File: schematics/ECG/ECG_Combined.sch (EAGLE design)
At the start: 76 parts, among them IC1 ADS1293, IC2 LIS3DH, IC3 MCP1703, IC4 CC2541, IC5 FSA4157, IC6 FSA4157, IC7 FSA4157, X1 XTAL-2SMD, X2 XTAL_403, X3 XTAL-CSM7

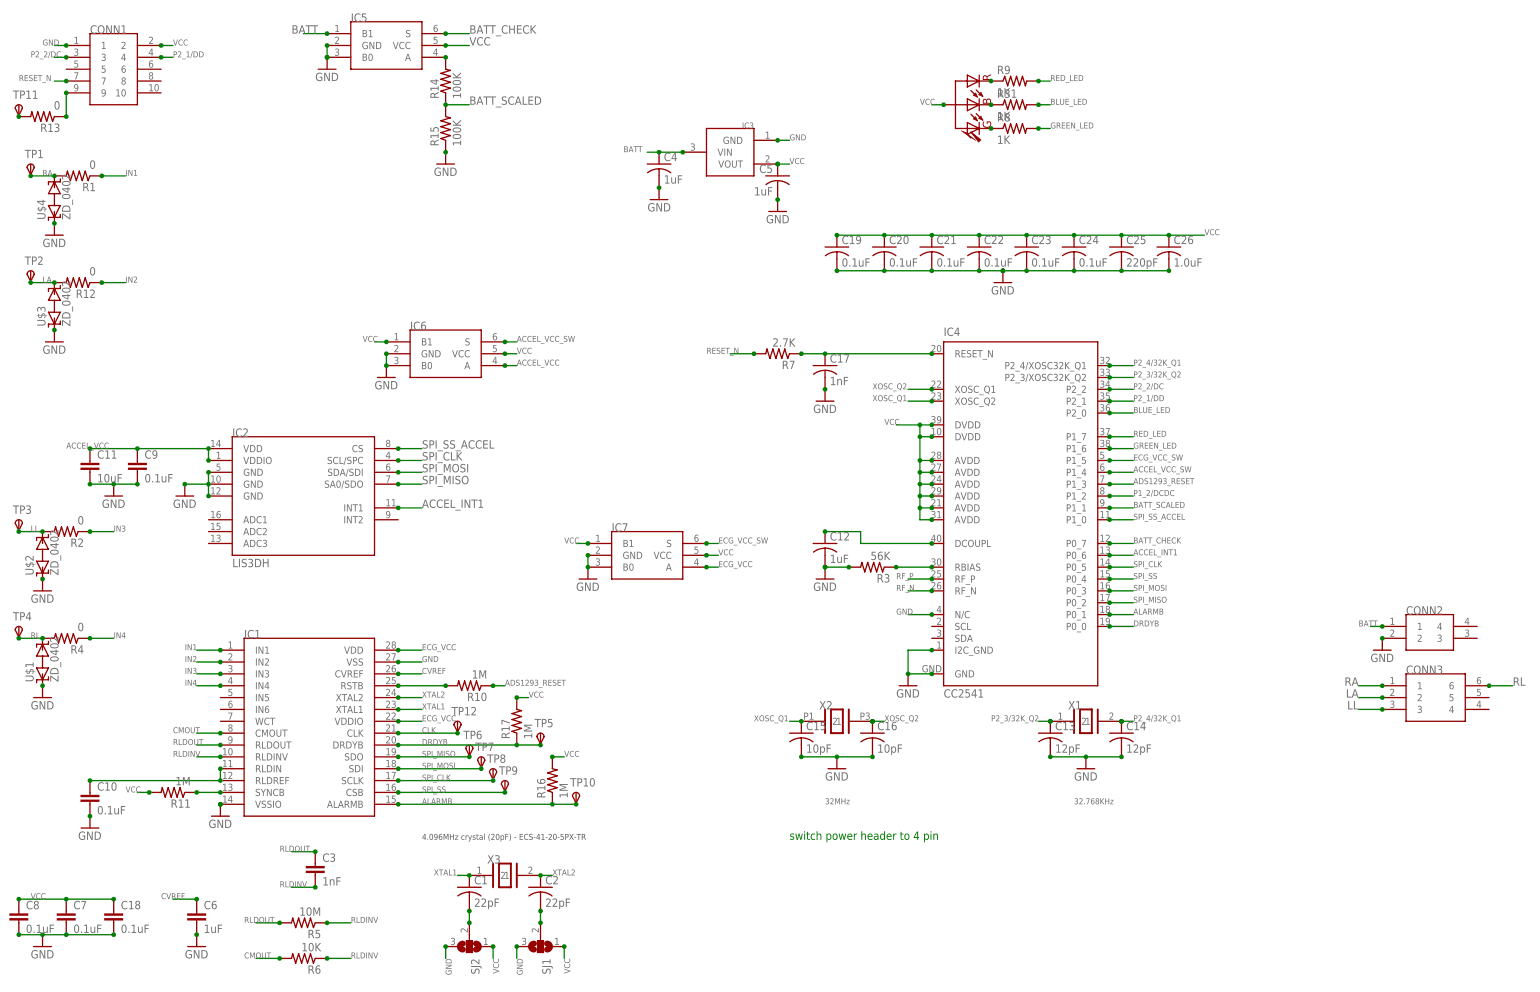
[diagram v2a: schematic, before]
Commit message: removed cc2541 ground on pin 4. added balun and antenna
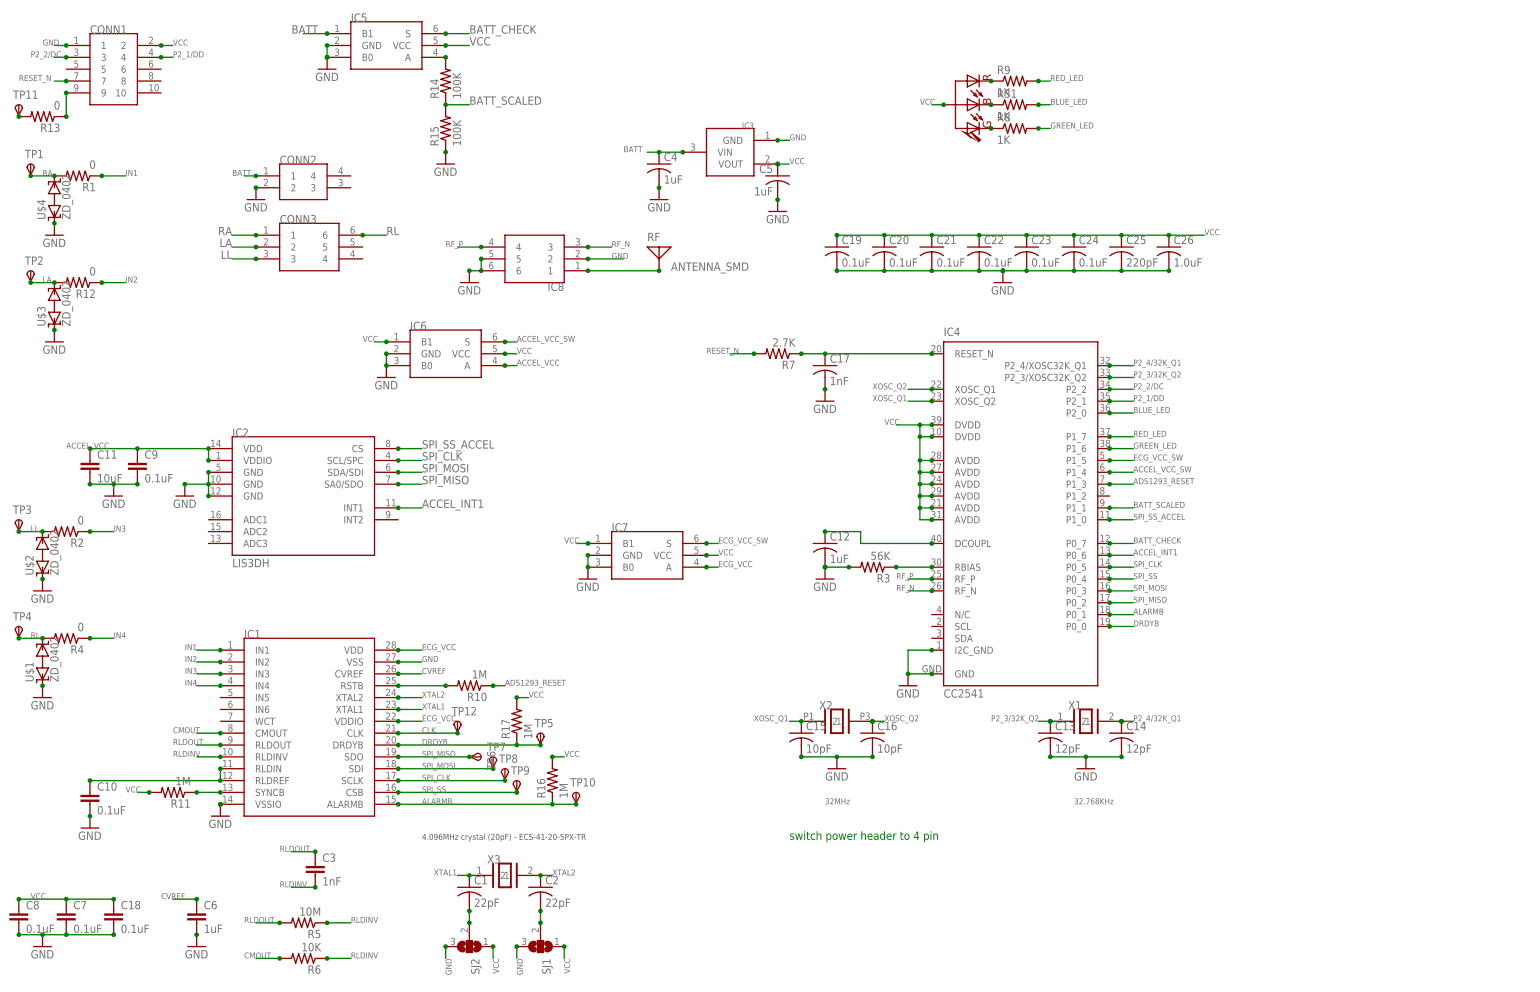
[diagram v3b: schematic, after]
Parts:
- added IC8: BALUN_2450BM_SERIES_SMD, johanson:BALUN_2450BM_SERIES_SMD
- added RF: ANTENNA_SMD, johanson:ANTENNA_SMD
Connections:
- net DCOUPL1 renamed DCOUPL
- removed net P1_2/DCDC: IC4.P1_2
- new net N$6: IC8.1, RF.1
- net GND: now also IC8.2, IC8.5, IC8.6; no longer IC4.N/C
- net RF_N: now also IC8.3
- net RF_P: now also IC8.4
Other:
- moved on the sheet: CONN2, CONN3, TP6, TP7, TP8, TP9
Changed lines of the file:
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@@
 <part name="GND20" library="supply1" deviceset="GND" device=""/>
 <part name="GND23" library="supply1" deviceset="GND" device=""/>
+<part name="RF" library="johanson" deviceset="ANTENNA_SMD" device=""/>
+<part name="IC8" library="johanson" deviceset="BALUN_2450BM_SERIES_SMD" device="" value=""/>
+<part name="GND24" library="supply1" deviceset="GND" device=""/>
 </parts>
 <sheets>
@@
 <instance part="TP4" gate="G$1" x="10.16" y="78.74"/>
 <instance part="TP5" gate="G$1" x="121.92" y="55.88"/>
-<instance part="TP6" gate="G$1" x="106.68" y="53.34"/>
-<instance part="TP7" gate="G$1" x="109.22" y="50.8"/>
-<instance part="TP8" gate="G$1" x="111.76" y="48.26"/>
-<instance part="TP9" gate="G$1" x="114.3" y="45.72"/>
+<instance part="TP6" gate="G$1" x="109.22" y="50.8" rot="R270"/>
+<instance part="TP7" gate="G$1" x="111.76" y="50.8"/>
+<instance part="TP8" gate="G$1" x="114.3" y="48.26"/>
+<instance part="TP9" gate="G$1" x="116.84" y="45.72"/>
 <instance part="TP10" gate="G$1" x="129.54" y="43.18"/>
 <instance part="R13" gate="G$1" x="15.24" y="187.96" rot="R180"/>
@@
 <instance part="R15" gate="G$1" x="101.6" y="185.42" rot="R90"/>
 <instance part="GND22" gate="1" x="101.6" y="177.8"/>
-<instance part="CONN3" gate="CONN" x="312.42" y="63.5"/>
+<instance part="CONN3" gate="CONN" x="71.12" y="160.02"/>
 <instance part="R1" gate="G$1" x="22.86" y="175.26" rot="R180"/>
 <instance part="R12" gate="G$1" x="22.86" y="152.4" rot="R180"/>
@@
 <instance part="TRI_LED" gate="LED" x="213.36" y="190.5" rot="R90"/>
 <instance part="R9" gate="G$1" x="223.52" y="195.58"/>
-<instance part="CONN2" gate="CONN" x="312.42" y="76.2"/>
-<instance part="GND17" gate="1" x="302.26" y="73.66"/>
+<instance part="CONN2" gate="CONN" x="71.12" y="172.72"/>
+<instance part="GND17" gate="1" x="60.96" y="170.18"/>
 <instance part="U$1" gate="Z" x="15.24" y="71.12" rot="R90"/>
 <instance part="U$2" gate="Z" x="15.24" y="93.98" rot="R90"/>
@@
 <instance part="GND20" gate="1" x="15.24" y="86.36"/>
 <instance part="GND23" gate="1" x="15.24" y="63.5"/>
+<instance part="RF" gate="RF" x="147.32" y="154.94"/>
+<instance part="IC8" gate="IC" x="121.92" y="157.48" rot="R180"/>
+<instance part="GND24" gate="1" x="106.68" y="152.4"/>
 </instances>
 <busses>
@@
 <junction x="205.74" y="73.66"/>
 <junction x="205.74" y="68.58"/>
-</segment>
-<segment>
-<pinref part="IC4" gate="G$1" pin="N/C"/>
-<junction x="205.74" y="81.28"/>
-<wire x1="205.74" y1="81.28" x2="200.66" y2="81.28" width="0.1524" layer="91"/>
-<label x="198.12" y="81.28" size="1.27" layer="95"/>
 </segment>
 <segment>
@@
 <pinref part="CONN2" gate="CONN" pin="2"/>
 <pinref part="GND17" gate="1" pin="GND"/>
-<junction x="302.26" y="76.2"/>
+<junction x="60.96" y="172.72"/>
 </segment>
 <segment>
@@
 <pinref part="GND23" gate="1" pin="GND"/>
 <junction x="15.24" y="66.04"/>
+</segment>
+<segment>
+<wire x1="109.22" y1="157.48" x2="109.22" y2="154.94" width="0.1524" layer="91"/>
+<wire x1="109.22" y1="154.94" x2="106.68" y2="154.94" width="0.1524" layer="91"/>
+<junction x="109.22" y="154.94"/>
+<junction x="109.22" y="157.48"/>
+<junction x="106.68" y="154.94"/>
+<pinref part="IC8" gate="IC" pin="5"/>
+<pinref part="IC8" gate="IC" pin="6"/>
+<pinref part="GND24" gate="1" pin="GND"/>
+</segment>
+<segment>
+<wire x1="132.08" y1="157.48" x2="139.7" y2="157.48" width="0.1524" layer="91"/>
+<junction x="132.08" y="157.48"/>
+<label x="137.16" y="157.48" size="1.27" layer="95"/>
+<pinref part="IC8" gate="IC" pin="2"/>
 </segment>
 </net>
@@
 <segment>
 <pinref part="CONN3" gate="CONN" pin="1"/>
-<junction x="302.26" y="66.04"/>
-<wire x1="302.26" y1="66.04" x2="297.18" y2="66.04" width="0.1524" layer="91"/>
-<label x="297.18" y="66.04" size="1.778" layer="95" rot="MR0"/>
+<junction x="60.96" y="162.56"/>
+<wire x1="60.96" y1="162.56" x2="55.88" y2="162.56" width="0.1524" layer="91"/>
+<label x="55.88" y="162.56" size="1.778" layer="95" rot="MR0"/>
 </segment>
 </net>
@@
 <segment>
 <pinref part="CONN3" gate="CONN" pin="3"/>
-<junction x="302.26" y="60.96"/>
-<wire x1="302.26" y1="60.96" x2="297.18" y2="60.96" width="0.1524" layer="91"/>
-<label x="297.18" y="60.96" size="1.778" layer="95" rot="MR0"/>
+<junction x="60.96" y="157.48"/>
+<wire x1="60.96" y1="157.48" x2="55.88" y2="157.48" width="0.1524" layer="91"/>
+<label x="55.88" y="157.48" size="1.778" layer="95" rot="MR0"/>
 </segment>
 </net>
@@
 <segment>
 <pinref part="CONN3" gate="CONN" pin="6"/>
-<junction x="325.12" y="66.04"/>
-<wire x1="325.12" y1="66.04" x2="330.2" y2="66.04" width="0.1524" layer="91"/>
-<label x="330.2" y="66.04" size="1.778" layer="95"/>
+<junction x="83.82" y="162.56"/>
+<wire x1="83.82" y1="162.56" x2="88.9" y2="162.56" width="0.1524" layer="91"/>
+<label x="88.9" y="162.56" size="1.778" layer="95"/>
 </segment>
 </net>
@@
 </segment>
 </net>
-<net name="DCOUPL1" class="0">
+<net name="DCOUPL" class="0">
 <segment>
 <pinref part="IC4" gate="G$1" pin="DCOUPL"/>
@@
 <label x="198.12" y="86.36" size="1.27" layer="95"/>
 </segment>
+<segment>
+<wire x1="137.16" y1="160.02" x2="132.08" y2="160.02" width="0.1524" layer="91"/>
+<junction x="132.08" y="160.02"/>
+<pinref part="IC8" gate="IC" pin="3"/>
+<label x="137.16" y="160.02" size="1.27" layer="95"/>
+</segment>
 </net>
 <net name="RF_P" class="0">
@@
 <label x="198.12" y="88.9" size="1.27" layer="95"/>
 </segment>
-</net>
-<net name="P1_2/DCDC" class="0">
-<segment>
-<pinref part="IC4" gate="G$1" pin="P1_2"/>
-<wire x1="243.84" y1="106.68" x2="248.92" y2="106.68" width="0.1524" layer="91"/>
-<junction x="243.84" y="106.68"/>
-<label x="248.92" y="106.68" size="1.27" layer="95"/>
+<segment>
+<wire x1="104.14" y1="160.02" x2="109.22" y2="160.02" width="0.1524" layer="91"/>
+<junction x="109.22" y="160.02"/>
+<pinref part="IC8" gate="IC" pin="4"/>
+<label x="101.6" y="160.02" size="1.27" layer="95"/>
 </segment>
 </net>
@@
 <junction x="91.44" y="48.26"/>
 <label x="96.52" y="48.26" size="1.27" layer="95"/>
-<wire x1="91.44" y1="48.26" x2="109.22" y2="48.26" width="0.1524" layer="91"/>
+<wire x1="91.44" y1="48.26" x2="111.76" y2="48.26" width="0.1524" layer="91"/>
 <pinref part="TP7" gate="G$1" pin="PP"/>
-<junction x="109.22" y="48.26"/>
+<junction x="111.76" y="48.26"/>
 </segment>
 </net>
@@
 <junction x="91.44" y="45.72"/>
 <label x="96.52" y="45.72" size="1.27" layer="95"/>
-<wire x1="91.44" y1="45.72" x2="111.76" y2="45.72" width="0.1524" layer="91"/>
+<wire x1="91.44" y1="45.72" x2="114.3" y2="45.72" width="0.1524" layer="91"/>
 <pinref part="TP8" gate="G$1" pin="PP"/>
-<junction x="111.76" y="45.72"/>
+<junction x="114.3" y="45.72"/>
 </segment>
 <segment>
@@
 <segment>
 <pinref part="IC1" gate="IC" pin="CSB"/>
-<wire x1="91.44" y1="43.18" x2="114.3" y2="43.18" width="0.1524" layer="91"/>
+<wire x1="91.44" y1="43.18" x2="116.84" y2="43.18" width="0.1524" layer="91"/>
 <junction x="91.44" y="43.18"/>
 <label x="96.52" y="43.18" size="1.27" layer="95"/>
 <pinref part="TP9" gate="G$1" pin="PP"/>
-<junction x="114.3" y="43.18"/>
+<junction x="116.84" y="43.18"/>
 </segment>
 <segment>
@@
 <segment>
 <pinref part="CONN3" gate="CONN" pin="2"/>
-<junction x="302.26" y="63.5"/>
-<wire x1="302.26" y1="63.5" x2="297.18" y2="63.5" width="0.1524" layer="91"/>
-<label x="297.18" y="63.5" size="1.778" layer="95" rot="MR0"/>
+<junction x="60.96" y="160.02"/>
+<wire x1="60.96" y1="160.02" x2="55.88" y2="160.02" width="0.1524" layer="91"/>
+<label x="55.88" y="160.02" size="1.778" layer="95" rot="MR0"/>
 </segment>
 </net>
@@
 <segment>
 <pinref part="CONN2" gate="CONN" pin="1"/>
-<wire x1="302.26" y1="78.74" x2="299.72" y2="78.74" width="0.1524" layer="91"/>
-<junction x="302.26" y="78.74"/>
-<label x="297.18" y="78.74" size="1.27" layer="95"/>
+<wire x1="60.96" y1="175.26" x2="58.42" y2="175.26" width="0.1524" layer="91"/>
+<junction x="60.96" y="175.26"/>
+<label x="55.88" y="175.26" size="1.27" layer="95"/>
 </segment>
 </net>
@@
 </segment>
 </net>
+<net name="N$6" class="0">
+<segment>
+<wire x1="132.08" y1="154.94" x2="147.32" y2="154.94" width="0.1524" layer="91"/>
+<junction x="132.08" y="154.94"/>
+<pinref part="IC8" gate="IC" pin="1"/>
+<pinref part="RF" gate="RF" pin="1"/>
+<junction x="147.32" y="154.94"/>
+</segment>
+</net>

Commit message: components placed in ideal positions for routing
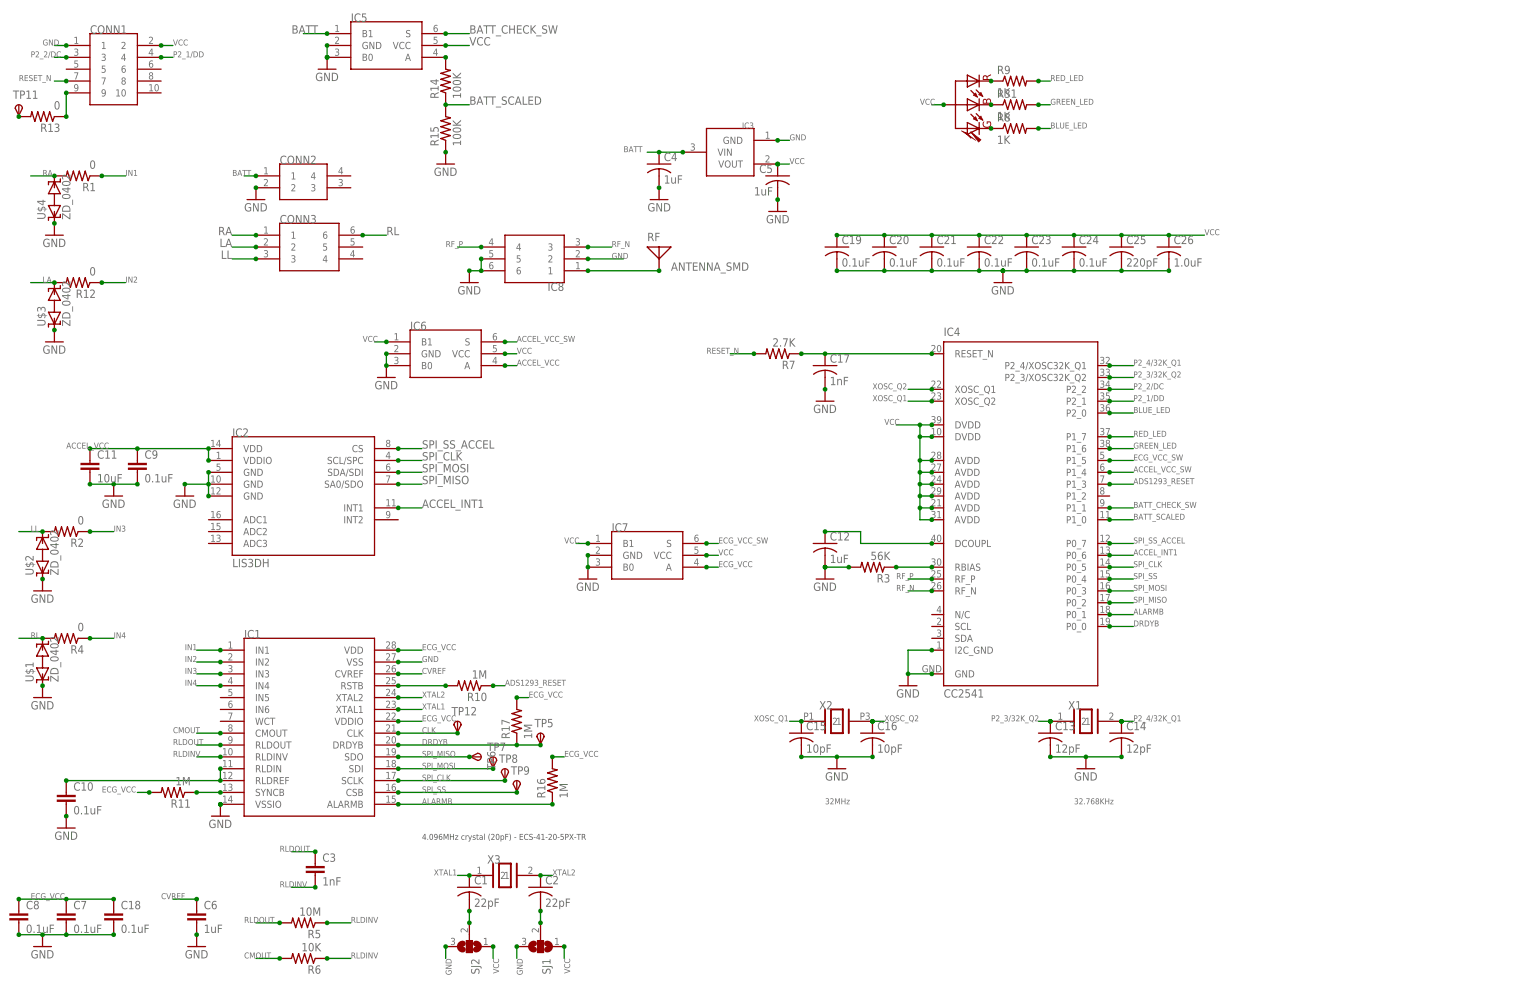
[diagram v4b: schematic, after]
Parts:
- removed TP1, TP10, TP2, TP3, TP4: TPSTP08SQ, testpad:TPSTP08SQ
- R31, R8, R9: device rcl:R-US_R0402 -> rcl:R-US_R0201
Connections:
- removed net BATT_CHECK: IC4.P0_7, IC5.S
- new net BATT_CHECK_SW: IC4.P1_1, IC5.S
- net ALARMB: no longer TP10.PP
- net BATT_SCALED: now also IC4.P1_0; no longer IC4.P1_1
- net BLUE_LED: now also R8.2; no longer R31.2
- net ECG_VCC: now also C18.1, C7.1, C8.1, R11.2, R16.2, R17.2
- net GREEN_LED: now also R31.2; no longer R8.2
- net LA: no longer TP2.PP
- net LL: no longer TP3.PP
- net RA: no longer TP1.PP
- net RL: no longer TP4.PP
- net SPI_SS_ACCEL: now also IC4.P0_7; no longer IC4.P1_0
- net VCC: no longer C18.1, C7.1, C8.1, R11.2, R16.2, R17.2
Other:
- note removed: "switch power header to 4 pin"
- moved on the sheet: C10

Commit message: continued routing
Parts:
- removed R13: 0, rcl:R-US_R0201
- removed SJ1, SJ2: (no value), jumper:SJ2W
- removed TP11: TPSTP08SQ, testpad:TPSTP08SQ
- added U$5: TC2030-MCP-NL, tagconnect:TC2030-MCP-NL
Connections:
- removed net N$1: CONN1.9, R13.1
- removed net N$10: C2.2, SJ1.2
- removed net N$13: C1.2, SJ2.2
- removed net N$2: R13.2, TP11.PP
- net ECG_VCC: now also C1.2, C2.2
- net GND: now also U$5.1; no longer SJ1.3, SJ2.3
- net P2_1/DD: now also U$5.5
- net P2_2/DC: now also U$5.2
- net RESET_N: now also U$5.3
- net VCC: now also U$5.4; no longer SJ1.1, SJ2.1

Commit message: board routed, still requires 50ohm ble antenna trace
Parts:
- added TP1: TPSTP08SQ, testpad:TPSTP08SQ
- TP12: value TPSTP08SQ -> TPSTP06R; device testpad:TPSTP08SQ -> testpad:TPSTP06R
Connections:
- net ADS1293_RESET: no longer R10.1
- net ALARMB: now also IC4.P0_0; no longer IC4.P0_1
- net DRDYB: now also IC4.P0_1; no longer IC4.P0_0
- net ECG_VCC: now also R10.1
- net LA: now also CONN3.1; no longer CONN3.2
- net LL: now also CONN3.6; no longer CONN3.3
- net RA: now also CONN3.2; no longer CONN3.1
- net RL: now also CONN3.5; no longer CONN3.6
- net SPI_SS_ACCEL: now also TP1.PP
